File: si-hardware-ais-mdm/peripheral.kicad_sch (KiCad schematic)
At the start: 11 parts, among them U10 L80-R, U2 24AA02E-OT, U7 LIS331HH

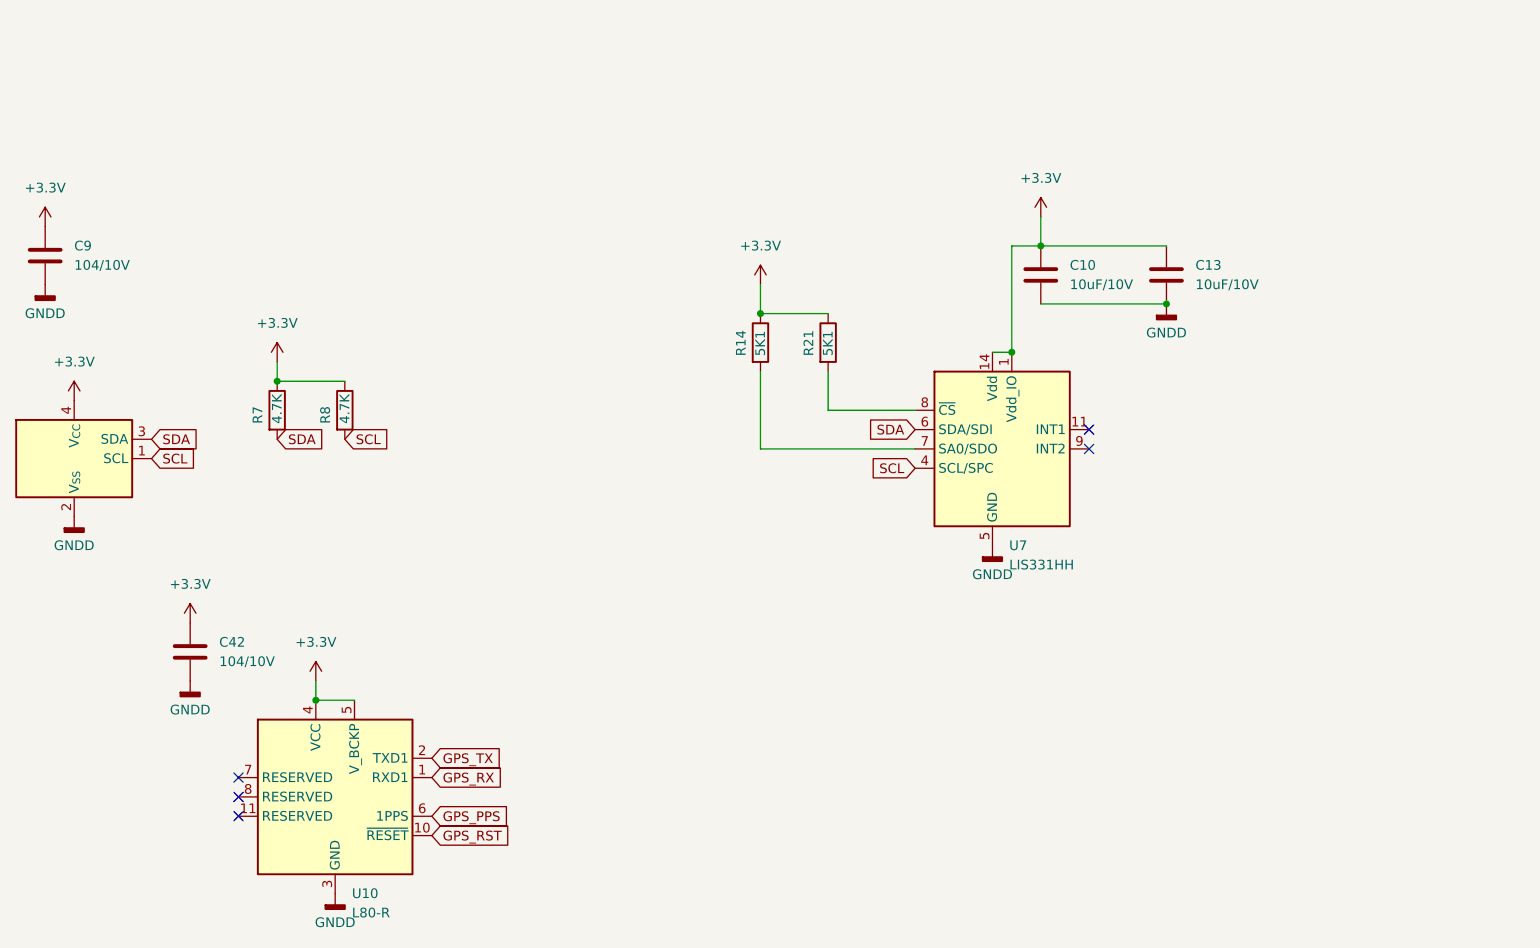
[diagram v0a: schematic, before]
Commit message: change mcu control
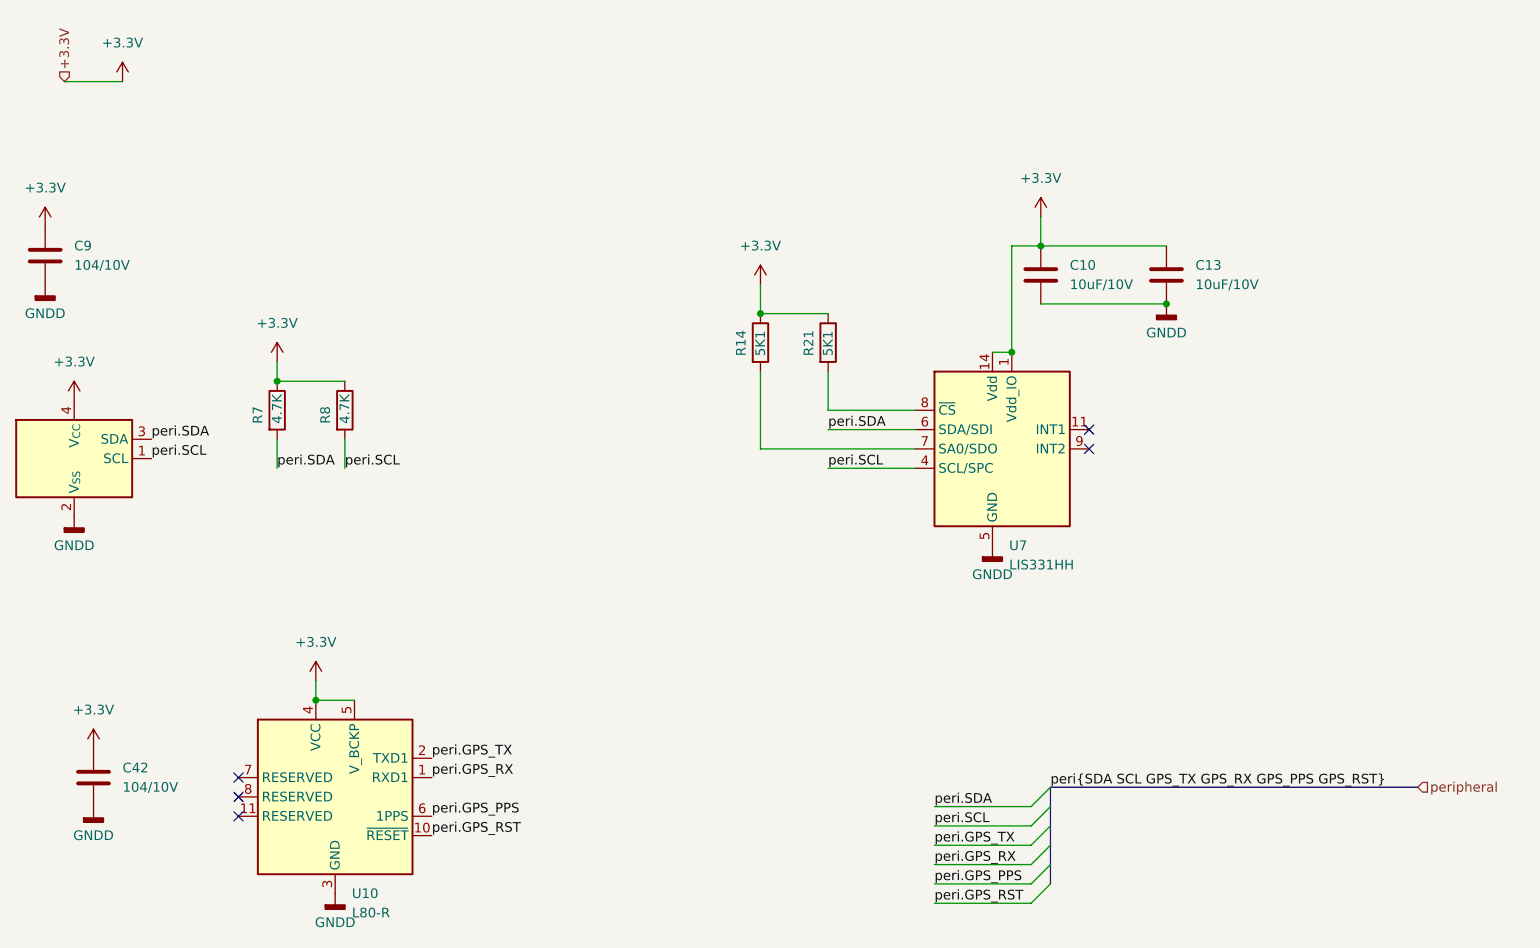
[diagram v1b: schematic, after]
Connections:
- net GPS_PPS renamed peri.GPS_PPS
- net GPS_RST renamed peri.GPS_RST
- net GPS_RX renamed peri.GPS_RX
- net GPS_TX renamed peri.GPS_TX
- net SCL renamed peri.SCL
- net SDA renamed peri.SDA
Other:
- moved on the sheet: C42
